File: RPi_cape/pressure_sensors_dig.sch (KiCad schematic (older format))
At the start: 11 parts, among them J17 Pressure_sensor_barb, J18 Pressure_sensor_barb, U10 MS5803-05BA, U14 BMP388

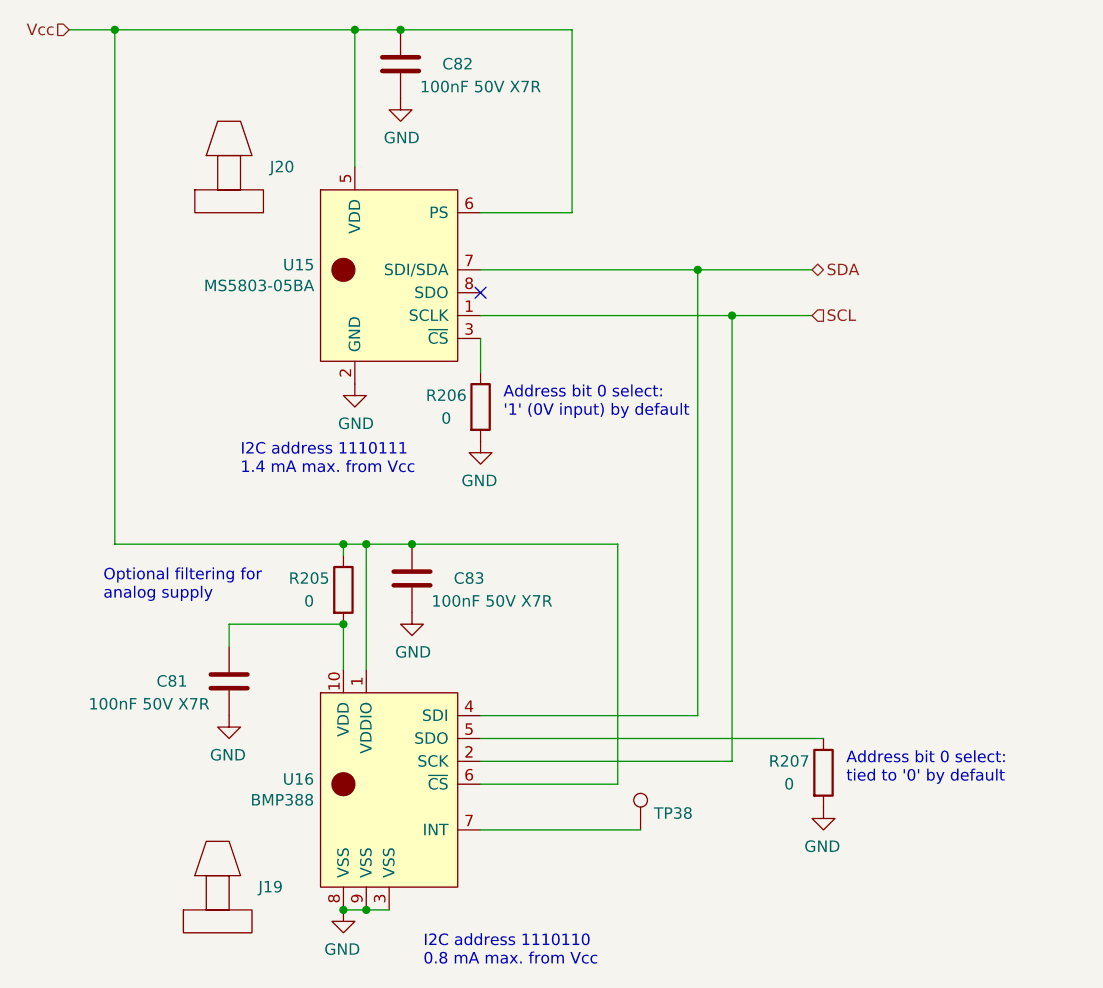
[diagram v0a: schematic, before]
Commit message: Better valve monitoring, finalized layout and manufacturing files
Created assembly and fabrication drawings, assigned all BOM parts, generally made design ready for ordering
Added strain-relief slots and barb mounting dimensions for digital pressure sensors
Changed valve drivers from discrete power MOSFETs to "smart" industrial/automotive driver ICs for the current monitoring, including valve-movement monitor for #4
Connected RPi_Valve* signals to larger CPLD footprint, changed Raspberry Pi pin assignment as a result to ease PCB routing
Updated footprints, page layout to create readable assembly drawing
Added current-measurement testpoints for CPLD power from BATT+
Changed power diodes in power-down-alarm circuit to small-signal parts for more compact layout
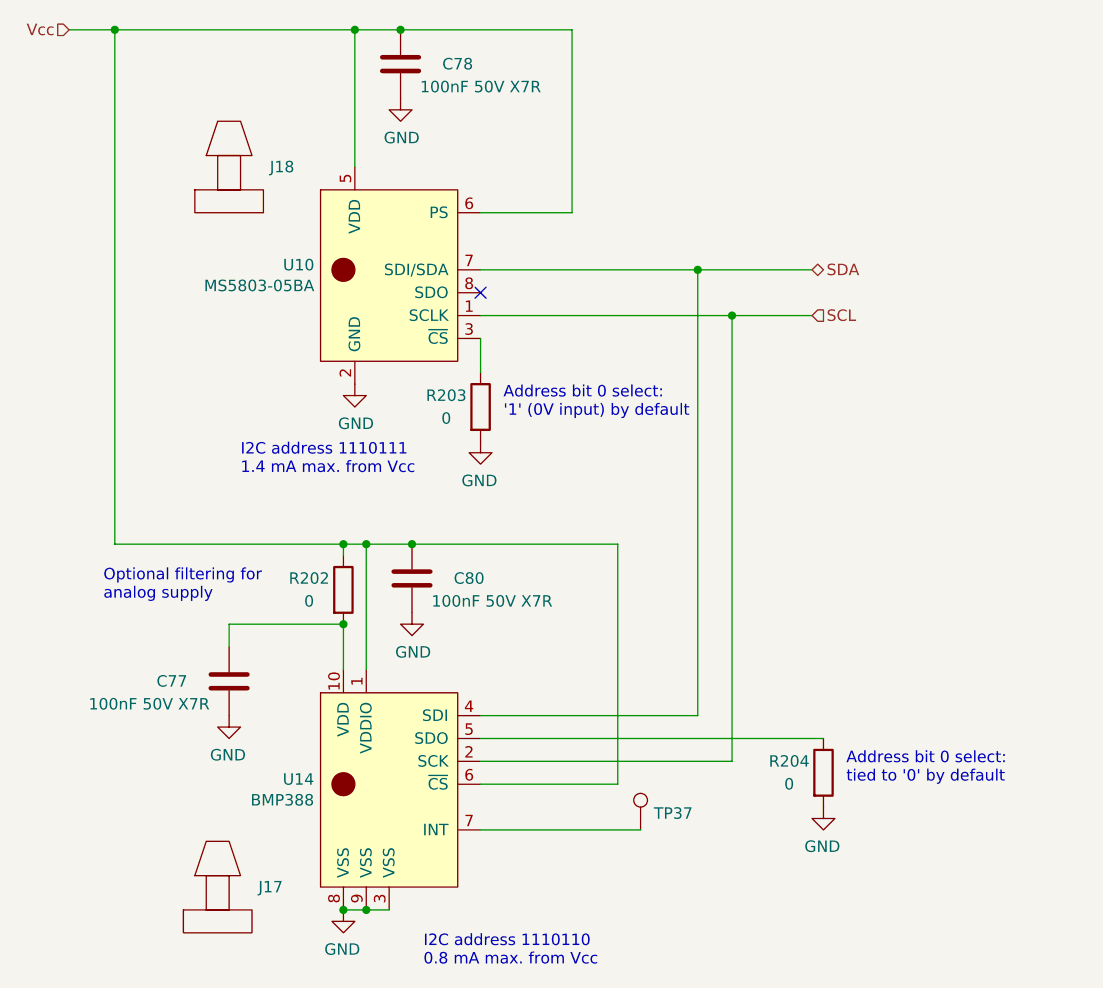
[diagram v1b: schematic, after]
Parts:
- J17, J18: footprint Ventilator:Pressure_sensor_barb -> Ventilator:Pressure_sensor_barb_inner-lip-expanded-slots
- R202, R203, R204: Manufacturer (none) -> Panasonic; Part Number (none) -> ERJ-8GEY0R00V
- U10: Manufacturer (none) -> TE; Part Number (none) -> MS5803-05BA01-00
- U14: footprint Ventilator:Bosch_BMP388_HandSolder -> Ventilator:Bosch_BMP388; Manufacturer (none) -> Bosch Sensortec; Part Number (none) -> BMP388
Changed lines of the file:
@@
 $Descr A4 11693 8268
 encoding utf-8
-Sheet 13 14
+Sheet 13 15
 Title ""
 Date ""
@@
 AR Path="/5F518E26/5F542369" Ref="U10"  Part="1"
 AR Path="/5F593E41/5F542369" Ref="U15"  Part="1"
-F 0 "U15" H 2123 2821 50  0000 R CNN
+F 0 "U10" H 2123 2821 50  0000 R CNN
 F 1 "MS5803-05BA" H 2123 2730 50  0000 R CNN
 F 2 "Ventilator:TE_MS5803-05BA" H 2450 2800 50  0001 C CNN
 F 3 "" H 2450 2800 50  0001 C CNN
+F 4 "TE" H 2450 2800 50  0001 C CNN "Manufacturer"
+F 5 "MS5803-05BA01-00" H 2450 2800 50  0001 C CNN "Part Number"
 	1    2450 2800
 	1    0    0    -1
@@
 AR Path="/5F518E26/5F542954" Ref="U14"  Part="1"
 AR Path="/5F593E41/5F542954" Ref="U16"  Part="1"
-F 0 "U16" H 2122 5071 50  0000 R CNN
+F 0 "U14" H 2122 5071 50  0000 R CNN
 F 1 "BMP388" H 2122 4980 50  0000 R CNN
-F 2 "Ventilator:Bosch_BMP388_HandSolder" H 2450 5100 50  0001 C CNN
+F 2 "Ventilator:Bosch_BMP388" H 2450 5100 50  0001 C CNN
 F 3 "" H 2450 5100 50  0001 C CNN
+F 4 "Bosch Sensortec" H 2450 5050 50  0001 C CNN "Manufacturer"
+F 5 "BMP388" H 2450 5050 50  0001 C CNN "Part Number"
 	1    2450 5050
 	1    0    0    -1
@@
 AR Path="/5F518E26/5F5543A0" Ref="C77"  Part="1"
 AR Path="/5F593E41/5F5543A0" Ref="C81"  Part="1"
-F 0 "C81" H 1500 4600 50  0000 C CNN
+F 0 "C77" H 1500 4600 50  0000 C CNN
 F 1 "100nF 50V X7R" H 1400 4700 50  0000 C CNN
 F 2 "Capacitor_SMD:C_0603_1608Metric" H 1788 4450 50  0001 C CNN
@@
 AR Path="/5F518E26/5F5543A6" Ref="#PWR0282"  Part="1"
 AR Path="/5F593E41/5F5543A6" Ref="#PWR0336"  Part="1"
-F 0 "#PWR0336" H 1750 4500 50  0001 C CNN
+F 0 "#PWR0282" H 1750 4500 50  0001 C CNN
 F 1 "GND" H 1755 4577 50  0000 C CNN
 F 2 "" H 1750 4750 50  0001 C CNN
@@
 AR Path="/5F518E26/5F5543B2" Ref="R202"  Part="1"
 AR Path="/5F593E41/5F5543B2" Ref="R205"  Part="1"
-F 0 "R205" H 2100 4250 50  0000 C CNN
+F 0 "R202" H 2100 4250 50  0000 C CNN
 F 1 "0" H 2100 4150 50  0000 C CNN
 F 2 "Resistor_SMD:R_1206_3216Metric" V 2180 4200 50  0001 C CNN
 F 3 "~" H 2250 4200 50  0001 C CNN
+F 4 "Panasonic" H 2250 4200 50  0001 C CNN "Manufacturer"
+F 5 "ERJ-8GEY0R00V" H 2250 4200 50  0001 C CNN "Part Number"
 	1    2250 4200
 	1    0    0    -1
@@
 AR Path="/5F518E26/5F55CEFC" Ref="C80"  Part="1"
 AR Path="/5F593E41/5F55CEFC" Ref="C83"  Part="1"
-F 0 "C83" H 2300 4150 50  0000 C CNN
+F 0 "C80" H 2300 4150 50  0000 C CNN
 F 1 "100nF 50V X7R" H 2200 4250 50  0000 C CNN
 F 2 "Capacitor_SMD:C_0603_1608Metric" H 2588 4000 50  0001 C CNN
@@
 AR Path="/5F518E26/5F55CF02" Ref="#PWR0285"  Part="1"
 AR Path="/5F593E41/5F55CF02" Ref="#PWR0337"  Part="1"
-F 0 "#PWR0337" H 2550 4050 50  0001 C CNN
+F 0 "#PWR0285" H 2550 4050 50  0001 C CNN
 F 1 "GND" H 2555 4127 50  0000 C CNN
 F 2 "" H 2550 4300 50  0001 C CNN
@@
 AR Path="/5F518E26/5F55E7E0" Ref="#PWR0286"  Part="1"
 AR Path="/5F593E41/5F55E7E0" Ref="#PWR0338"  Part="1"
-F 0 "#PWR0338" H 2250 5350 50  0001 C CNN
+F 0 "#PWR0286" H 2250 5350 50  0001 C CNN
 F 1 "GND" H 2255 5427 50  0000 C CNN
 F 2 "" H 2250 5600 50  0001 C CNN
@@
 AR Path="/5F518E26/5F560E40" Ref="C78"  Part="1"
 AR Path="/5F593E41/5F560E40" Ref="C82"  Part="1"
-F 0 "C82" H 2250 1900 50  0000 C CNN
+F 0 "C78" H 2250 1900 50  0000 C CNN
 F 1 "100nF 50V X7R" H 2150 2000 50  0000 C CNN
 F 2 "Capacitor_SMD:C_0603_1608Metric" H 2538 1750 50  0001 C CNN
@@
 AR Path="/5F518E26/5F560E46" Ref="#PWR0332"  Part="1"
 AR Path="/5F593E41/5F560E46" Ref="#PWR0339"  Part="1"
-F 0 "#PWR0339" H 2500 1800 50  0001 C CNN
+F 0 "#PWR0332" H 2500 1800 50  0001 C CNN
 F 1 "GND" H 2505 1877 50  0000 C CNN
 F 2 "" H 2500 2050 50  0001 C CNN
@@
 AR Path="/5F518E26/5F5615BC" Ref="#PWR0333"  Part="1"
 AR Path="/5F593E41/5F5615BC" Ref="#PWR0340"  Part="1"
-F 0 "#PWR0340" H 2300 3050 50  0001 C CNN
+F 0 "#PWR0333" H 2300 3050 50  0001 C CNN
 F 1 "GND" H 2305 3127 50  0000 C CNN
 F 2 "" H 2300 3300 50  0001 C CNN
@@
 AR Path="/5F518E26/5F56BBEF" Ref="R204"  Part="1"
 AR Path="/5F593E41/5F56BBEF" Ref="R207"  Part="1"
-F 0 "R207" H 4200 5050 50  0000 C CNN
+F 0 "R204" H 4200 5050 50  0000 C CNN
 F 1 "0" H 4200 4950 50  0000 C CNN
 F 2 "Resistor_SMD:R_1206_3216Metric" V 4280 5000 50  0001 C CNN
 F 3 "~" H 4350 5000 50  0001 C CNN
+F 4 "Panasonic" H 4350 5000 50  0001 C CNN "Manufacturer"
+F 5 "ERJ-8GEY0R00V" H 4350 5000 50  0001 C CNN "Part Number"
 	1    4350 5000
 	1    0    0    -1
@@
 AR Path="/5F518E26/5F56CAA8" Ref="#PWR0334"  Part="1"
 AR Path="/5F593E41/5F56CAA8" Ref="#PWR0341"  Part="1"
-F 0 "#PWR0341" H 4350 4900 50  0001 C CNN
+F 0 "#PWR0334" H 4350 4900 50  0001 C CNN
 F 1 "GND" H 4355 4977 50  0000 C CNN
 F 2 "" H 4350 5150 50  0001 C CNN
@@
 AR Path="/5F518E26/5F570F1D" Ref="TP37"  Part="1"
 AR Path="/5F593E41/5F570F1D" Ref="TP38"  Part="1"
-F 0 "TP38" H 3608 5322 50  0000 L CNN
+F 0 "TP37" H 3608 5322 50  0000 L CNN
 F 1 "TestPoint" H 3608 5277 50  0001 L CNN
 F 2 "TestPoint:TestPoint_Pad_2.0x2.0mm" H 3750 5250 50  0001 C CNN
@@
 AR Path="/5F518E26/5F5769F4" Ref="R203"  Part="1"
 AR Path="/5F593E41/5F5769F4" Ref="R206"  Part="1"
-F 0 "R206" H 2700 3450 50  0000 C CNN
+F 0 "R203" H 2700 3450 50  0000 C CNN
 F 1 "0" H 2700 3350 50  0000 C CNN
 F 2 "Resistor_SMD:R_1206_3216Metric" V 2780 3400 50  0001 C CNN
 F 3 "~" H 2850 3400 50  0001 C CNN
+F 4 "Panasonic" H 2850 3400 50  0001 C CNN "Manufacturer"
+F 5 "ERJ-8GEY0R00V" H 2850 3400 50  0001 C CNN "Part Number"
 	1    2850 3400
 	1    0    0    -1
@@
 AR Path="/5F518E26/5F5769FA" Ref="#PWR0335"  Part="1"
 AR Path="/5F593E41/5F5769FA" Ref="#PWR0342"  Part="1"
-F 0 "#PWR0342" H 2850 3300 50  0001 C CNN
+F 0 "#PWR0335" H 2850 3300 50  0001 C CNN
 F 1 "GND" H 2855 3377 50  0000 C CNN
 F 2 "" H 2850 3550 50  0001 C CNN
@@
 AR Path="/5F518E26/5F666F01" Ref="J18"  Part="1"
 AR Path="/5F593E41/5F666F01" Ref="J20"  Part="1"
-F 0 "J20" H 1928 2650 50  0000 L CNN
+F 0 "J18" H 1928 2650 50  0000 L CNN
 F 1 "Pressure_sensor_barb" H 1700 2850 50  0001 C CNN
-F 2 "Ventilator:Pressure_sensor_barb" H 1750 2500 50  0001 C CNN
+F 2 "Ventilator:Pressure_sensor_barb_inner-lip-expanded-slots" H 1750 2500 50  0001 C CNN
 F 3 "" H 1750 2500 50  0001 C CNN
 	1    1750 2500
@@
 AR Path="/5F518E26/5F667549" Ref="J17"  Part="1"
 AR Path="/5F593E41/5F667549" Ref="J19"  Part="1"
-F 0 "J19" H 1878 5800 50  0000 L CNN
+F 0 "J17" H 1878 5800 50  0000 L CNN
 F 1 "Pressure_sensor_barb" H 1650 6000 50  0001 C CNN
-F 2 "Ventilator:Pressure_sensor_barb" H 1700 5650 50  0001 C CNN
+F 2 "Ventilator:Pressure_sensor_barb_inner-lip-expanded-slots" H 1700 5650 50  0001 C CNN
 F 3 "" H 1700 5650 50  0001 C CNN
 	1    1700 5650

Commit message: Safety additions
Switched CPLD_ADC7 to +24V monitoring (from +5V monitoring), and added CPLD ~Bat_On digital input(s) to know when it's running from backup battery, to cover low-input-voltage edge cases
Added series 1K resistors (R226-231) on CPLD<->RPi Comms1-6 lines, to protect CPLD in case of overvoltage from RPi failure
Added optional input TVS D23 to handle sustained over-voltage or large surges
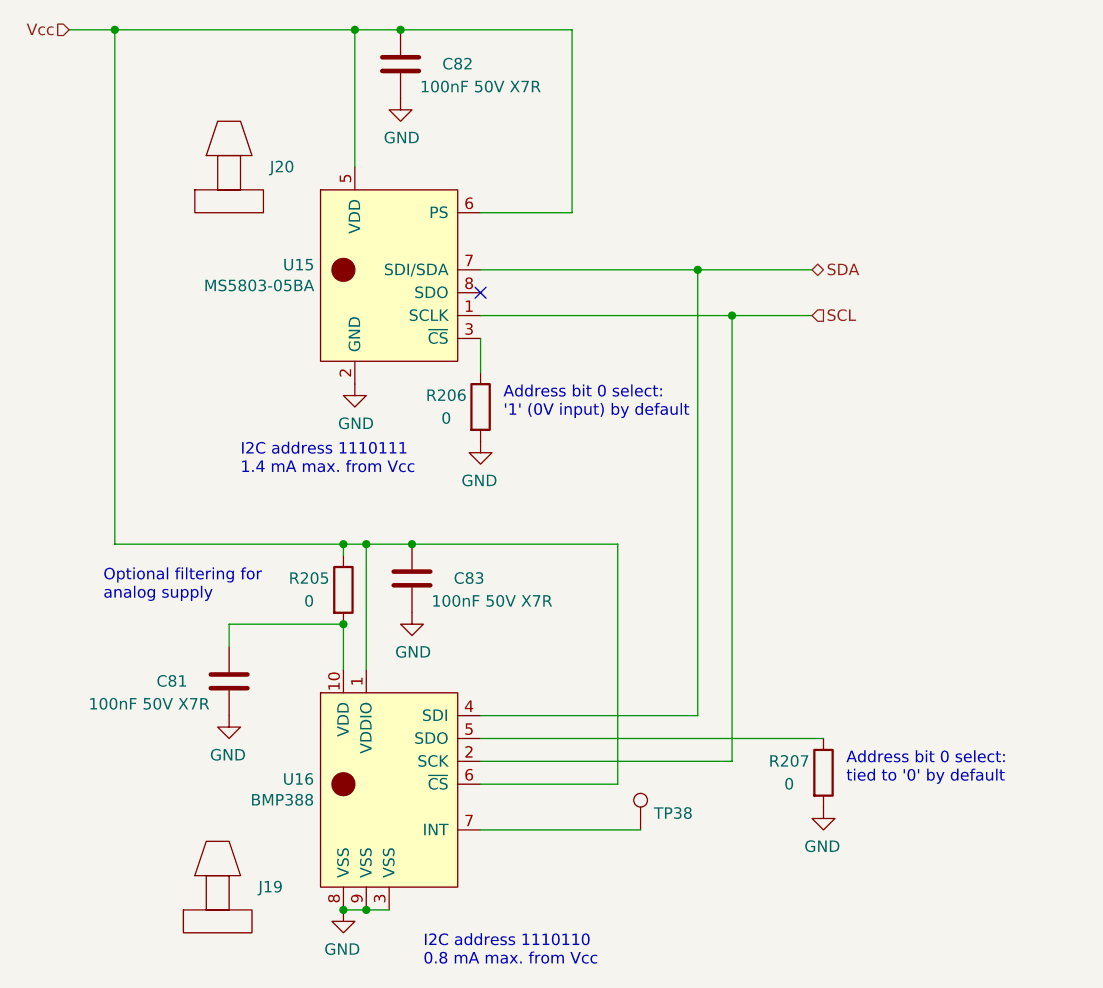
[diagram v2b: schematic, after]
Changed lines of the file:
@@
 AR Path="/5F518E26/5F542369" Ref="U10"  Part="1"
 AR Path="/5F593E41/5F542369" Ref="U15"  Part="1"
-F 0 "U10" H 2123 2821 50  0000 R CNN
+F 0 "U15" H 2123 2821 50  0000 R CNN
 F 1 "MS5803-05BA" H 2123 2730 50  0000 R CNN
 F 2 "Ventilator:TE_MS5803-05BA" H 2450 2800 50  0001 C CNN
@@
 AR Path="/5F518E26/5F542954" Ref="U14"  Part="1"
 AR Path="/5F593E41/5F542954" Ref="U16"  Part="1"
-F 0 "U14" H 2122 5071 50  0000 R CNN
+F 0 "U16" H 2122 5071 50  0000 R CNN
 F 1 "BMP388" H 2122 4980 50  0000 R CNN
 F 2 "Ventilator:Bosch_BMP388" H 2450 5100 50  0001 C CNN
@@
 AR Path="/5F518E26/5F5543A0" Ref="C77"  Part="1"
 AR Path="/5F593E41/5F5543A0" Ref="C81"  Part="1"
-F 0 "C77" H 1500 4600 50  0000 C CNN
+F 0 "C81" H 1500 4600 50  0000 C CNN
 F 1 "100nF 50V X7R" H 1400 4700 50  0000 C CNN
 F 2 "Capacitor_SMD:C_0603_1608Metric" H 1788 4450 50  0001 C CNN
@@
 AR Path="/5F518E26/5F5543A6" Ref="#PWR0282"  Part="1"
 AR Path="/5F593E41/5F5543A6" Ref="#PWR0336"  Part="1"
-F 0 "#PWR0282" H 1750 4500 50  0001 C CNN
+F 0 "#PWR0336" H 1750 4500 50  0001 C CNN
 F 1 "GND" H 1755 4577 50  0000 C CNN
 F 2 "" H 1750 4750 50  0001 C CNN
@@
 AR Path="/5F518E26/5F5543B2" Ref="R202"  Part="1"
 AR Path="/5F593E41/5F5543B2" Ref="R205"  Part="1"
-F 0 "R202" H 2100 4250 50  0000 C CNN
+F 0 "R205" H 2100 4250 50  0000 C CNN
 F 1 "0" H 2100 4150 50  0000 C CNN
 F 2 "Resistor_SMD:R_1206_3216Metric" V 2180 4200 50  0001 C CNN
@@
 AR Path="/5F518E26/5F55CEFC" Ref="C80"  Part="1"
 AR Path="/5F593E41/5F55CEFC" Ref="C83"  Part="1"
-F 0 "C80" H 2300 4150 50  0000 C CNN
+F 0 "C83" H 2300 4150 50  0000 C CNN
 F 1 "100nF 50V X7R" H 2200 4250 50  0000 C CNN
 F 2 "Capacitor_SMD:C_0603_1608Metric" H 2588 4000 50  0001 C CNN
@@
 AR Path="/5F518E26/5F55CF02" Ref="#PWR0285"  Part="1"
 AR Path="/5F593E41/5F55CF02" Ref="#PWR0337"  Part="1"
-F 0 "#PWR0285" H 2550 4050 50  0001 C CNN
+F 0 "#PWR0337" H 2550 4050 50  0001 C CNN
 F 1 "GND" H 2555 4127 50  0000 C CNN
 F 2 "" H 2550 4300 50  0001 C CNN
@@
 AR Path="/5F518E26/5F55E7E0" Ref="#PWR0286"  Part="1"
 AR Path="/5F593E41/5F55E7E0" Ref="#PWR0338"  Part="1"
-F 0 "#PWR0286" H 2250 5350 50  0001 C CNN
+F 0 "#PWR0338" H 2250 5350 50  0001 C CNN
 F 1 "GND" H 2255 5427 50  0000 C CNN
 F 2 "" H 2250 5600 50  0001 C CNN
@@
 AR Path="/5F518E26/5F560E40" Ref="C78"  Part="1"
 AR Path="/5F593E41/5F560E40" Ref="C82"  Part="1"
-F 0 "C78" H 2250 1900 50  0000 C CNN
+F 0 "C82" H 2250 1900 50  0000 C CNN
 F 1 "100nF 50V X7R" H 2150 2000 50  0000 C CNN
 F 2 "Capacitor_SMD:C_0603_1608Metric" H 2538 1750 50  0001 C CNN
@@
 AR Path="/5F518E26/5F560E46" Ref="#PWR0332"  Part="1"
 AR Path="/5F593E41/5F560E46" Ref="#PWR0339"  Part="1"
-F 0 "#PWR0332" H 2500 1800 50  0001 C CNN
+F 0 "#PWR0339" H 2500 1800 50  0001 C CNN
 F 1 "GND" H 2505 1877 50  0000 C CNN
 F 2 "" H 2500 2050 50  0001 C CNN
@@
 AR Path="/5F518E26/5F5615BC" Ref="#PWR0333"  Part="1"
 AR Path="/5F593E41/5F5615BC" Ref="#PWR0340"  Part="1"
-F 0 "#PWR0333" H 2300 3050 50  0001 C CNN
+F 0 "#PWR0340" H 2300 3050 50  0001 C CNN
 F 1 "GND" H 2305 3127 50  0000 C CNN
 F 2 "" H 2300 3300 50  0001 C CNN
@@
 AR Path="/5F518E26/5F56BBEF" Ref="R204"  Part="1"
 AR Path="/5F593E41/5F56BBEF" Ref="R207"  Part="1"
-F 0 "R204" H 4200 5050 50  0000 C CNN
+F 0 "R207" H 4200 5050 50  0000 C CNN
 F 1 "0" H 4200 4950 50  0000 C CNN
 F 2 "Resistor_SMD:R_1206_3216Metric" V 4280 5000 50  0001 C CNN
@@
 AR Path="/5F518E26/5F56CAA8" Ref="#PWR0334"  Part="1"
 AR Path="/5F593E41/5F56CAA8" Ref="#PWR0341"  Part="1"
-F 0 "#PWR0334" H 4350 4900 50  0001 C CNN
+F 0 "#PWR0341" H 4350 4900 50  0001 C CNN
 F 1 "GND" H 4355 4977 50  0000 C CNN
 F 2 "" H 4350 5150 50  0001 C CNN
@@
 AR Path="/5F518E26/5F570F1D" Ref="TP37"  Part="1"
 AR Path="/5F593E41/5F570F1D" Ref="TP38"  Part="1"
-F 0 "TP37" H 3608 5322 50  0000 L CNN
+F 0 "TP38" H 3608 5322 50  0000 L CNN
 F 1 "TestPoint" H 3608 5277 50  0001 L CNN
 F 2 "TestPoint:TestPoint_Pad_2.0x2.0mm" H 3750 5250 50  0001 C CNN
@@
 AR Path="/5F518E26/5F5769F4" Ref="R203"  Part="1"
 AR Path="/5F593E41/5F5769F4" Ref="R206"  Part="1"
-F 0 "R203" H 2700 3450 50  0000 C CNN
+F 0 "R206" H 2700 3450 50  0000 C CNN
 F 1 "0" H 2700 3350 50  0000 C CNN
 F 2 "Resistor_SMD:R_1206_3216Metric" V 2780 3400 50  0001 C CNN
@@
 AR Path="/5F518E26/5F5769FA" Ref="#PWR0335"  Part="1"
 AR Path="/5F593E41/5F5769FA" Ref="#PWR0342"  Part="1"
-F 0 "#PWR0335" H 2850 3300 50  0001 C CNN
+F 0 "#PWR0342" H 2850 3300 50  0001 C CNN
 F 1 "GND" H 2855 3377 50  0000 C CNN
 F 2 "" H 2850 3550 50  0001 C CNN
@@
 AR Path="/5F518E26/5F666F01" Ref="J18"  Part="1"
 AR Path="/5F593E41/5F666F01" Ref="J20"  Part="1"
-F 0 "J18" H 1928 2650 50  0000 L CNN
+F 0 "J20" H 1928 2650 50  0000 L CNN
 F 1 "Pressure_sensor_barb" H 1700 2850 50  0001 C CNN
 F 2 "Ventilator:Pressure_sensor_barb_inner-lip-expanded-slots" H 1750 2500 50  0001 C CNN
@@
 AR Path="/5F518E26/5F667549" Ref="J17"  Part="1"
 AR Path="/5F593E41/5F667549" Ref="J19"  Part="1"
-F 0 "J17" H 1878 5800 50  0000 L CNN
+F 0 "J19" H 1878 5800 50  0000 L CNN
 F 1 "Pressure_sensor_barb" H 1650 6000 50  0001 C CNN
 F 2 "Ventilator:Pressure_sensor_barb_inner-lip-expanded-slots" H 1700 5650 50  0001 C CNN
